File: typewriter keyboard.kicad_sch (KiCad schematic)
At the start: 82 parts, among them J1 Conn_01x11_Male, J2 Conn_01x08_Male, J3 Raspberry_Pi_2_3, SW1 SW_Push, SW10 SW_Push, SW11 SW_Push, SW12 SW_Push, SW13 SW_Push, SW14 SW_Push, SW15 SW_Push, SW16 SW_Push, SW17 SW_Push, SW18 SW_Push, SW19 SW_Push, SW2 SW_Push, SW20 SW_Push, SW21 SW_Push, SW22 SW_Push, SW23 SW_Push, SW24 SW_Push, SW25 SW_Push, SW26 SW_Push, SW27 SW_Push, SW28 SW_Push, SW29 SW_Push, SW3 SW_Push, SW30 SW_Push, SW31 SW_Push, SW32 SW_Push, SW33 SW_Push, SW34 SW_Push, SW35 SW_Push, SW36 SW_Push, SW37 SW_Push, SW38 SW_Push, SW39 SW_Push, SW4 SW_Push, SW40 SW_Push, SW41 SW_Push, SW42 SW_Push, SW43 SW_Push, SW44 SW_Push, SW45 SW_Push, SW46 SW_Push, SW47 SW_Push, SW48 SW_Push, SW49 SW_Push, SW5 SW_Push, SW50 SW_Push, SW51 SW_Push, SW52 SW_Push, SW53 SW_Push, SW54 SW_Push, SW55 SW_Push, SW56 SW_Push, SW57 SW_Push, SW58 SW_Push, SW59 SW_Push, SW6 SW_Push, SW60 SW_Push, SW61 SW_Push, SW62 SW_Push, SW63 SW_Push, SW64 SW_Push, SW65 SW_Push, SW66 SW_Push, SW67 SW_Push, SW68 SW_Push, SW69 SW_Push, SW7 SW_Push, SW70 SW_Push, SW8 SW_Push, SW9 SW_Push, U1 CD74HC4067SM, U2 CD74HC4067SM, U3 CD74HC4067SM, U4 CD74HC4067SM, U5 Arduino_Nano

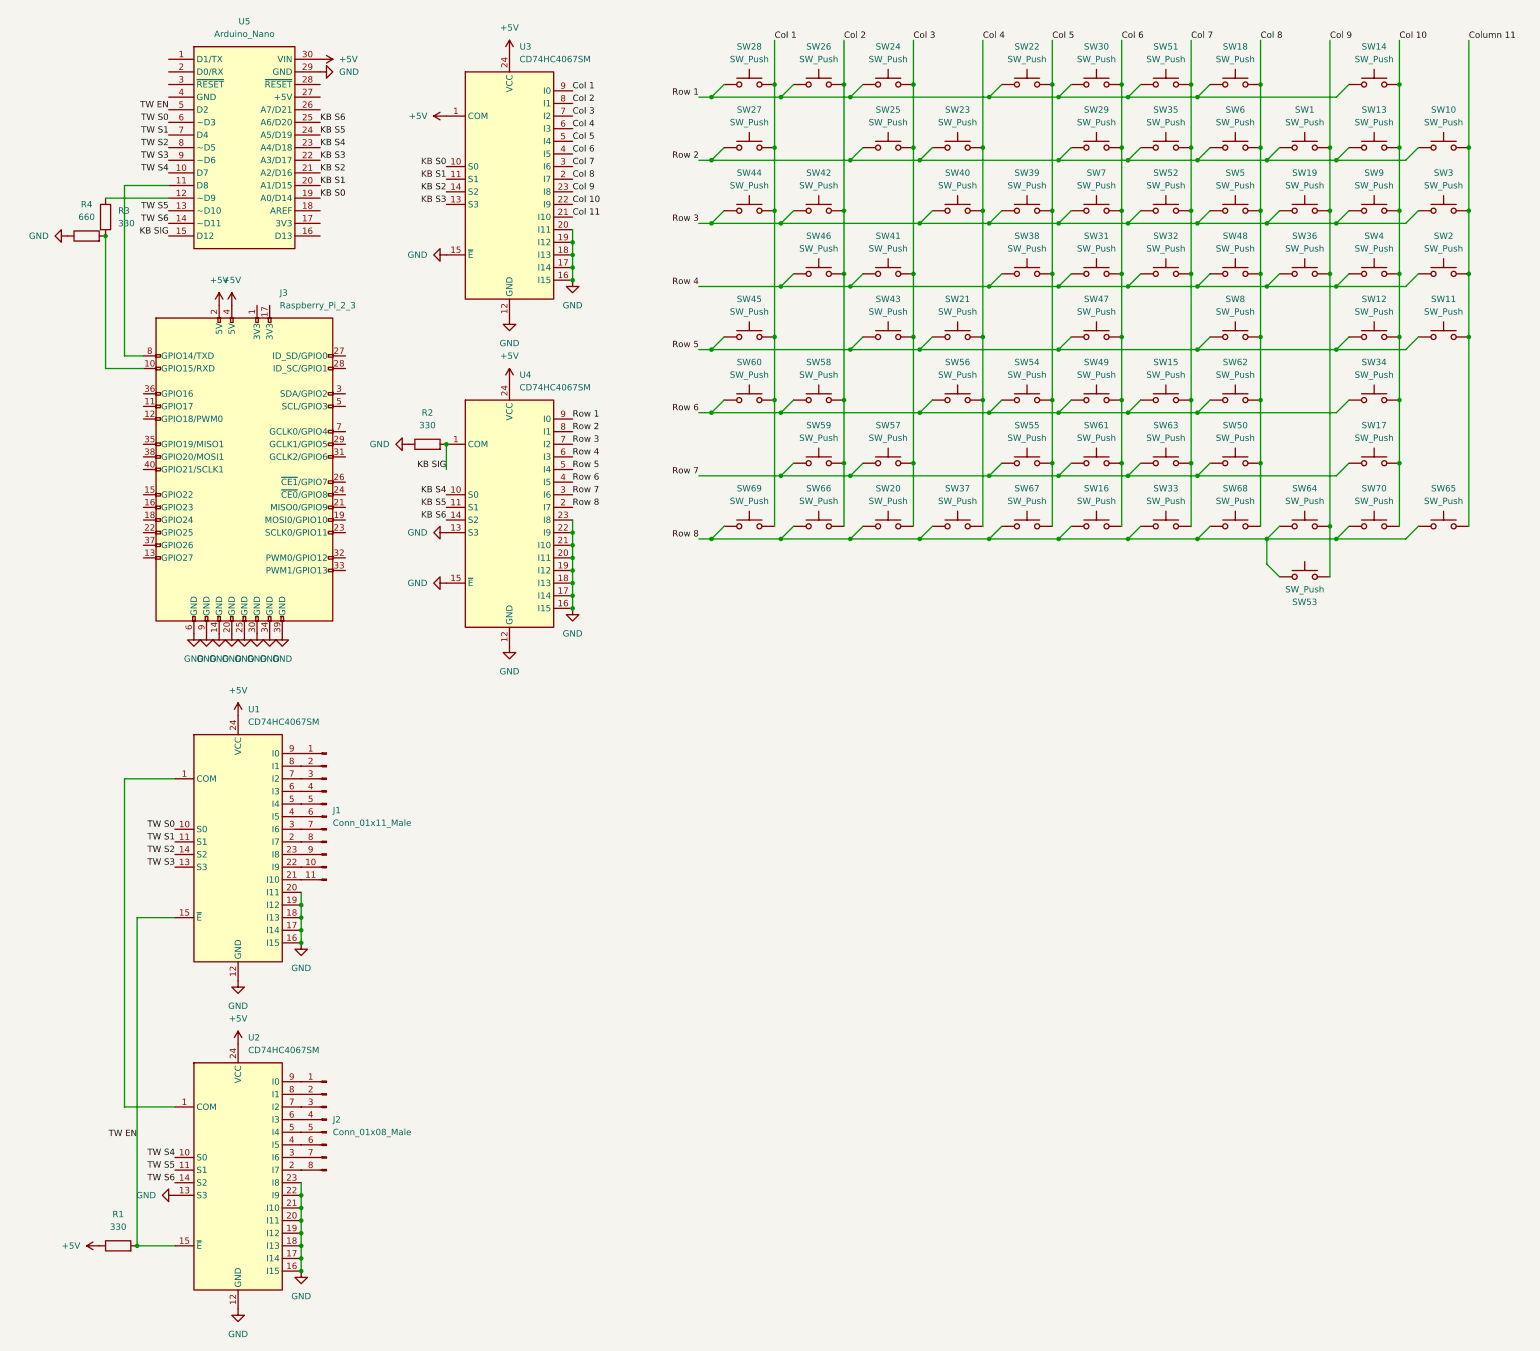
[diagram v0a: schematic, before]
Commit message: Routed PCB, cleaned up schematic
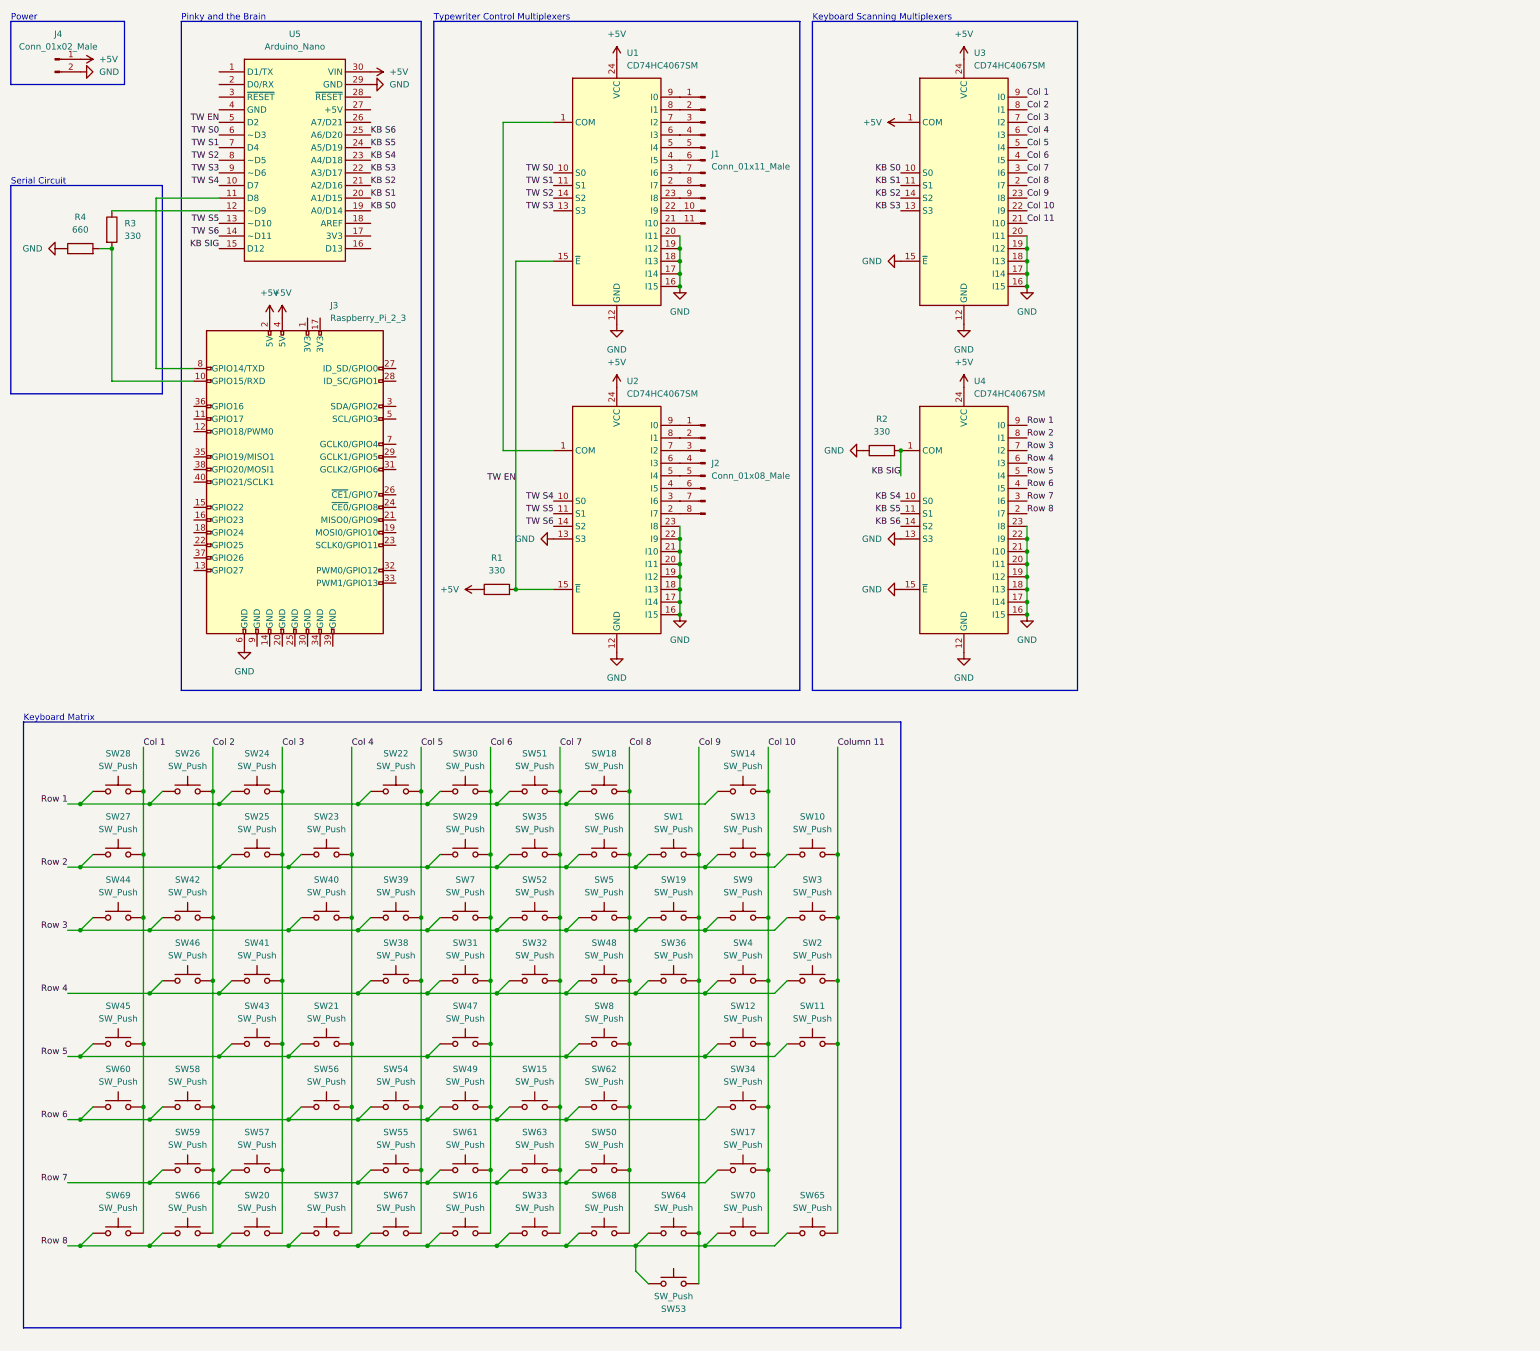
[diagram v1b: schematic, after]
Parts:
- added J4: Conn_01x02_Male, Connector_Wire:SolderWire-0.1sqmm_1x02_P3.6mm_D0.4mm_OD1mm, symbol Connector:Conn_01x02_Male
- SW1, SW10, SW11, SW12, SW13, SW14, SW15, SW17, SW18, SW19, SW2, SW21, SW22, SW23, SW24, SW25, SW26, SW27, SW28, SW29, SW3, SW30, SW31, SW32, SW34, SW35, SW36, SW38, SW39, SW4, SW40, SW41, SW42, SW43, SW44, SW45, SW46, SW47, SW48, SW5, SW50, SW51, SW52, SW54, SW55, SW56, SW57, SW58, SW59, SW6, SW60, SW61, SW62, SW63, SW65, SW7, SW8, SW9: footprint Alps_Only:ALPS-1U -> MX_Alps_Hybrid:MX-1U-NoLED
- SW16: footprint Alps_Only:ALPS-2U -> MX_Alps_Hybrid:MX-2U-NoLED
- SW20, SW33: footprint Alps_Only:ALPS-1.5U -> MX_Alps_Hybrid:MX-1.5U-NoLED
- SW37: footprint Alps_Only:ALPS-1.75U -> MX_Alps_Hybrid:MX-1.75U-NoLED
- SW49, SW53: footprint Alps_Only:ALPS-2.25U -> MX_Alps_Hybrid:MX-2.25U-NoLED
- SW64: footprint Alps_Only:ALPS-2.75U -> MX_Alps_Hybrid:MX-2.75U-NoLED
- SW66, SW67, SW69, SW70: footprint Alps_Only:ALPS-1.25U -> MX_Alps_Hybrid:MX-1.25U-NoLED
- SW68: footprint Alps_Only:ALPS-6.25U -> MX_Alps_Hybrid:MX-6.25U-NoLED
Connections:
- net +5V: now also J4.1 (Pin_1)
- net GND: now also J4.2 (Pin_2); no longer J3.14 (GND), J3.20 (GND), J3.25 (GND), J3.30 (GND), J3.34 (GND), J3.39 (GND), J3.9 (GND)
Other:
- note added: "Keyboard Matrix"
- note added: "Keyboard Scanning Multiplexers"
- note added: "Pinky and the Brain"
- note added: "Power"
- note added: "Serial Circuit"
- note added: "Typewriter Control Multiplexers"
- moved on the sheet: J1, J2, J3, R1, R2, R3, R4, SW1, SW10, SW11, SW12, SW13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

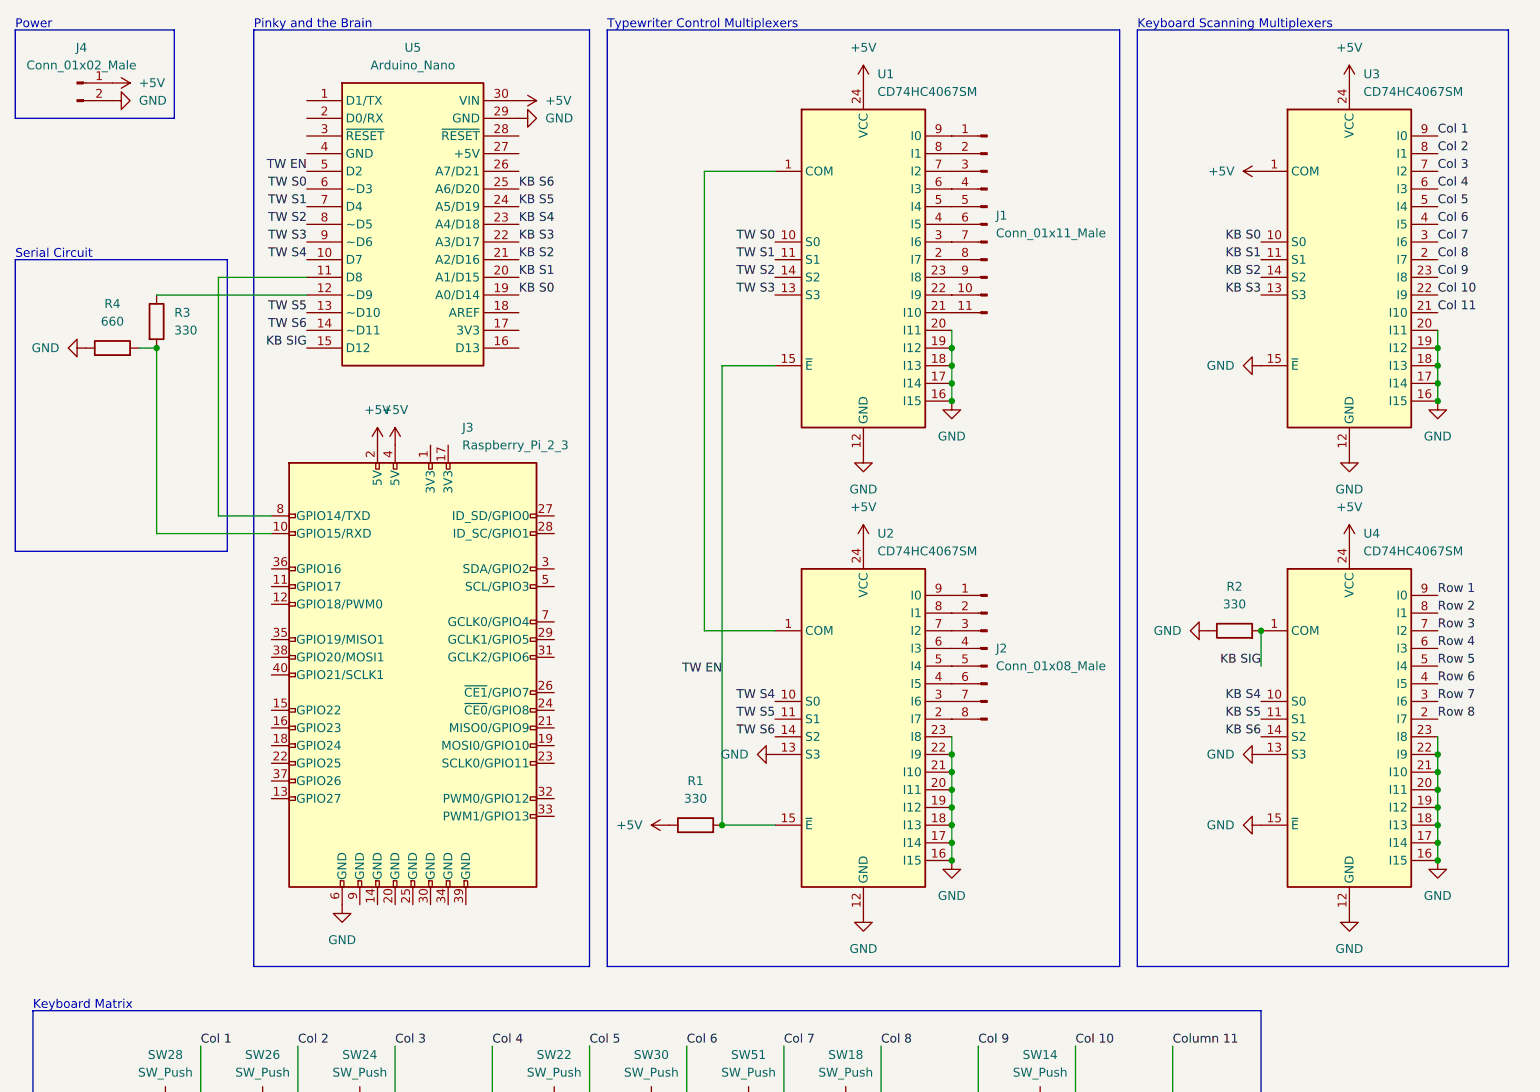
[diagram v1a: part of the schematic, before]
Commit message: Cleaned up schematic and board
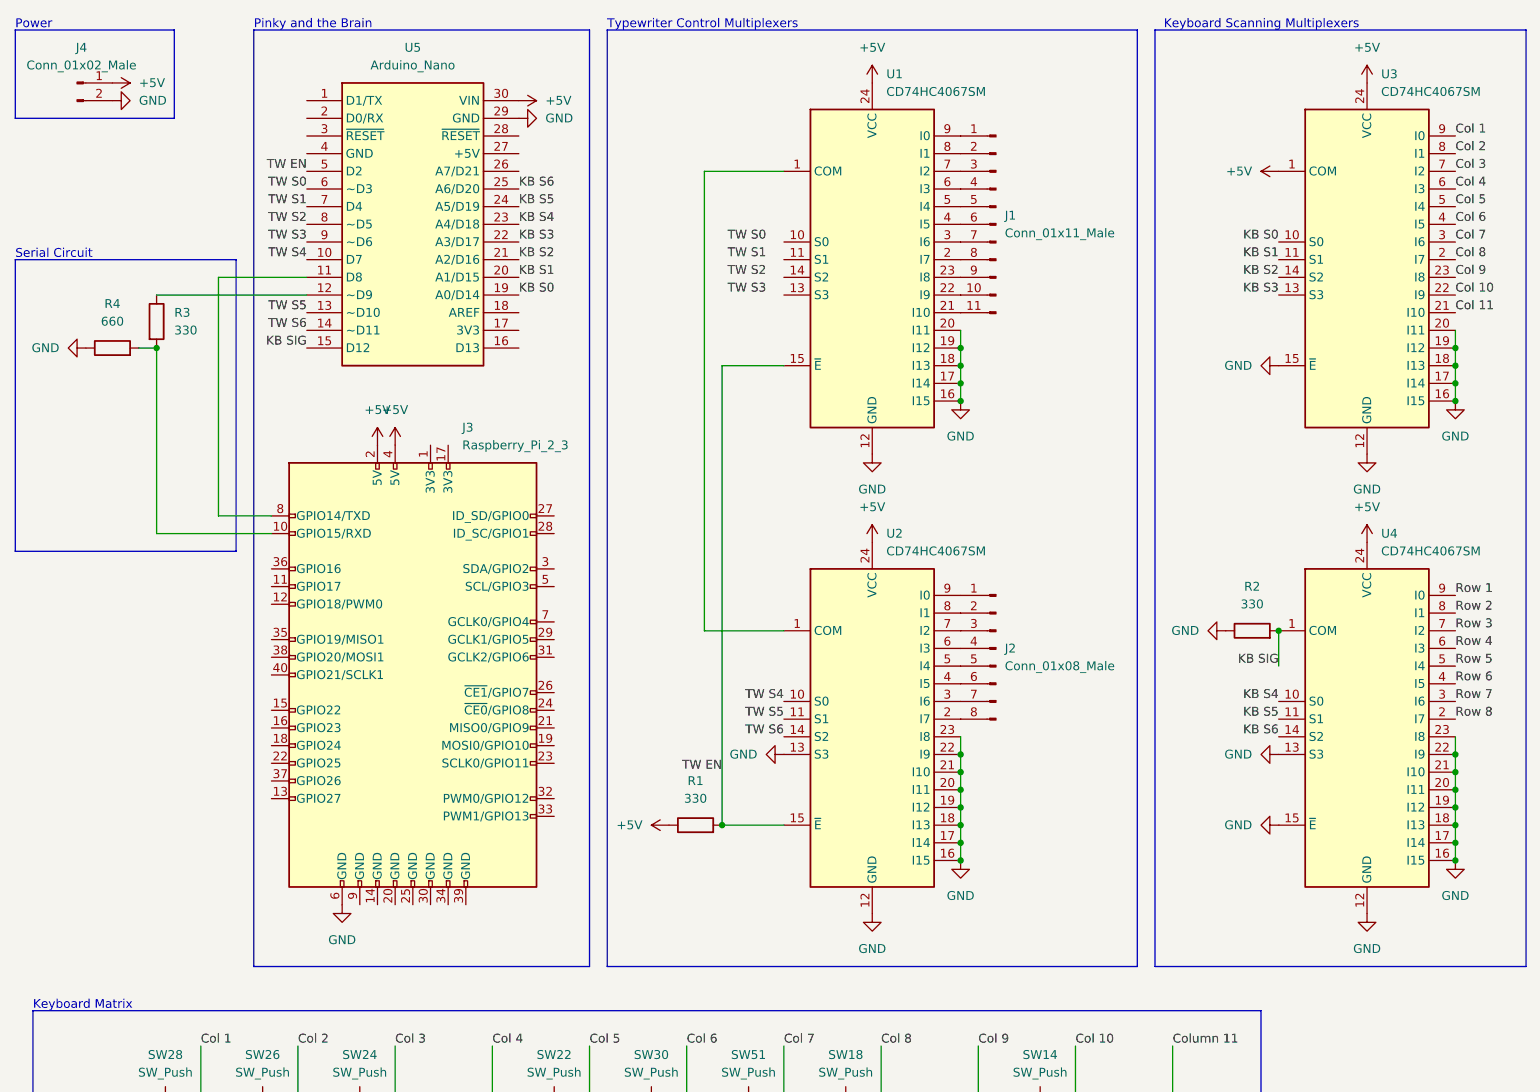
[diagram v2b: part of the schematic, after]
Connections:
- net TW S0: no longer U1.10 (S0)
- net TW S1: no longer U1.11 (S1)
- net TW S2: no longer U1.14 (S2)
- net TW S3: no longer U1.13 (S3)
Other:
- title: (none) -> Brother AX-25 Serial Terminal Control Board
- moved on the sheet: J1, J2, R2, U1, U2, U3, U4

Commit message: Final changes for order
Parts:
- removed J4: Conn_01x02_Male, Connector_Wire:SolderWire-0.1sqmm_1x02_P3.6mm_D0.4mm_OD1mm, symbol Connector:Conn_01x02_Male
- added +5V1, GND1: Conn_01x01_Male, Connector_Wire:SolderWire-0.25sqmm_1x01_D0.65mm_OD1.7mm, symbol Connector:Conn_01x01_Male
- added C1, C2, C3, C4: 100u, Capacitor_THT:C_Disc_D3.4mm_W2.1mm_P2.50mm, symbol Device:C
- added R5: 330, Resistor_THT:R_Axial_DIN0207_L6.3mm_D2.5mm_P10.16mm_Horizontal, symbol Device:R
- R4: value 660 -> 330
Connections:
- net +5V: now also U5.27 (+5V), +5V1.1 (Pin_1), C1.1, C2.1, C3.1, C4.1; no longer U5.30 (VIN)
- net GND: now also C1.2, C2.2, C3.2, C4.2, GND1.1 (Pin_1)
- net TW S0: now also U1.10 (S0)
- net TW S1: now also U1.11 (S1)
- net TW S2: now also U1.14 (S2)
- net TW S3: now also U1.13 (S3)
- net at J3.10 (GPIO15/RXD), R3.2: now also R5.2; no longer R4.2
- new net: R4.2, R5.1
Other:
- moved on the sheet: J1, J2, R1, R2, U1, U2, U3, U4
